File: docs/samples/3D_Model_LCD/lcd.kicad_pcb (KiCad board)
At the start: 2 copper layers, 97.6 x 48.2 mm, 2 parts, among them J1 Conn_01x12_Female

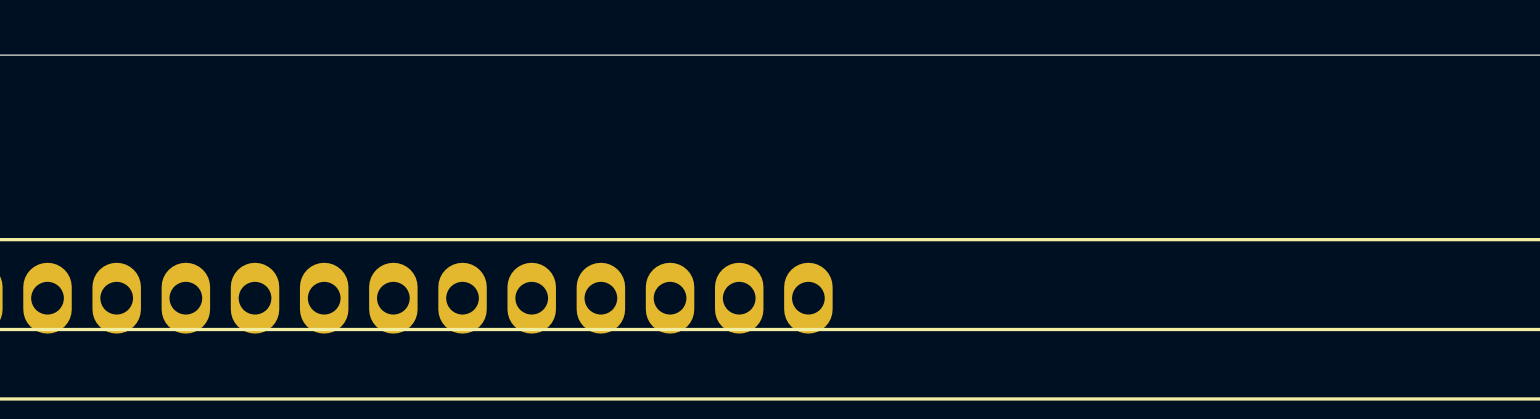
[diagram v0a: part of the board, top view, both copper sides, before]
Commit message: [Examples] 3D model variant LCD example migrated to KiCad 9
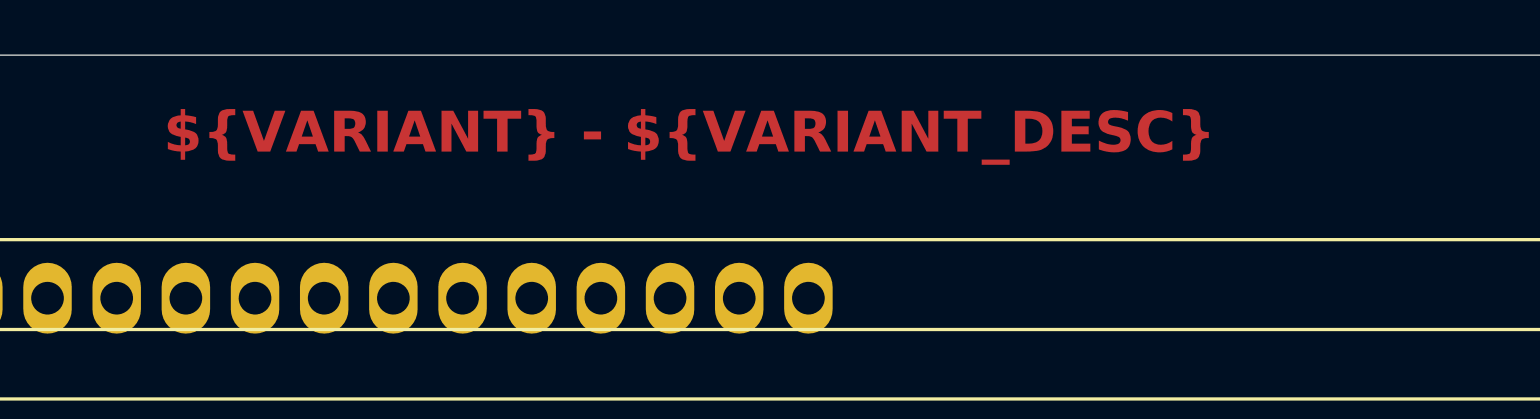
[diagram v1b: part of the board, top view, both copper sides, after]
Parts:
- DS1001: value **Val -> LCD16x02
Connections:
- DS1001 pad 1: Net-(DS1001-Pad1) -> unconnected-(DS1001-VSS-Pad1)
- DS1001 pad 10: Net-(DS1001-Pad10) -> unconnected-(DS1001-D3-Pad10)
- DS1001 pad 11: Net-(DS1001-Pad11) -> unconnected-(DS1001-D4-Pad11)
- DS1001 pad 12: Net-(DS1001-Pad12) -> unconnected-(DS1001-D5-Pad12)
- DS1001 pad 13: Net-(DS1001-Pad13) -> unconnected-(DS1001-D6-Pad13)
- DS1001 pad 14: Net-(DS1001-Pad14) -> unconnected-(DS1001-D7-Pad14)
- DS1001 pad 15: Net-(DS1001-Pad15) -> unconnected-(DS1001-LED(+)-Pad15)
- DS1001 pad 16: Net-(DS1001-Pad16) -> unconnected-(DS1001-LED(-)-Pad16)
- DS1001 pad 2: Net-(DS1001-Pad2) -> unconnected-(DS1001-VDD-Pad2)
- DS1001 pad 3: Net-(DS1001-Pad3) -> unconnected-(DS1001-VO-Pad3)
- DS1001 pad 4: Net-(DS1001-Pad4) -> unconnected-(DS1001-RS-Pad4)
- DS1001 pad 5: Net-(DS1001-Pad5) -> unconnected-(DS1001-R/W-Pad5)
- DS1001 pad 6: Net-(DS1001-Pad6) -> unconnected-(DS1001-E-Pad6)
- DS1001 pad 7: Net-(DS1001-Pad7) -> unconnected-(DS1001-D0-Pad7)
- DS1001 pad 8: Net-(DS1001-Pad8) -> unconnected-(DS1001-D1-Pad8)
- DS1001 pad 9: Net-(DS1001-Pad9) -> unconnected-(DS1001-D2-Pad9)
- J1 pad 1: Net-(J1-Pad1) -> unconnected-(J1-Pin_1-Pad1)
- J1 pad 10: Net-(J1-Pad10) -> unconnected-(J1-Pin_10-Pad10)
- J1 pad 11: Net-(J1-Pad11) -> unconnected-(J1-Pin_11-Pad11)
- J1 pad 12: Net-(J1-Pad12) -> unconnected-(J1-Pin_12-Pad12)
- J1 pad 2: Net-(J1-Pad2) -> unconnected-(J1-Pin_2-Pad2)
- J1 pad 3: Net-(J1-Pad3) -> unconnected-(J1-Pin_3-Pad3)
- J1 pad 4: Net-(J1-Pad4) -> unconnected-(J1-Pin_4-Pad4)
- J1 pad 5: Net-(J1-Pad5) -> unconnected-(J1-Pin_5-Pad5)
- J1 pad 6: Net-(J1-Pad6) -> unconnected-(J1-Pin_6-Pad6)
- J1 pad 7: Net-(J1-Pad7) -> unconnected-(J1-Pin_7-Pad7)
- J1 pad 8: Net-(J1-Pad8) -> unconnected-(J1-Pin_8-Pad8)
- J1 pad 9: Net-(J1-Pad9) -> unconnected-(J1-Pin_9-Pad9)
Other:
- board text added: "${VARIANT} - ${VARIANT_DESC}"
